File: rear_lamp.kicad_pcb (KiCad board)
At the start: 2 copper layers, 20.3 x 15.4 mm, 9 parts, among them J1 PWR, Q1 BD137

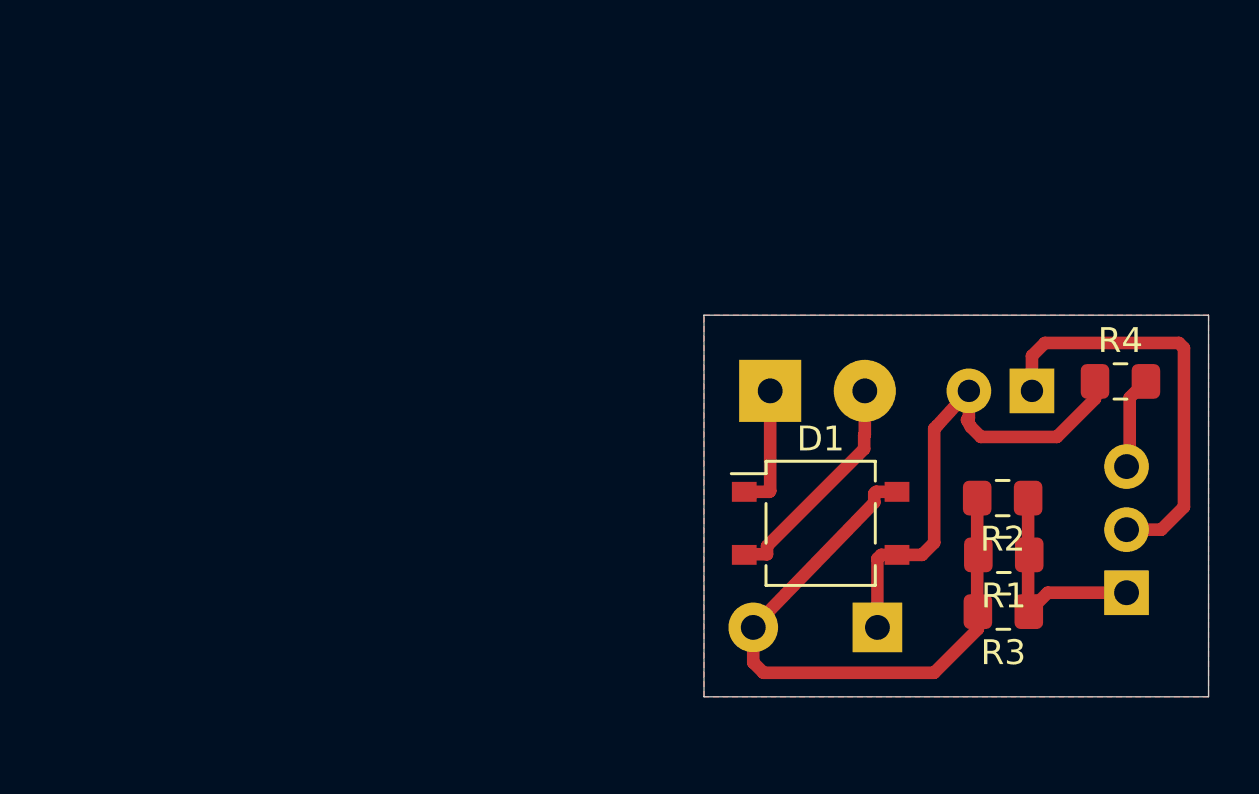
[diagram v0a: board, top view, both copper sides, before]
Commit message: discrete led driver
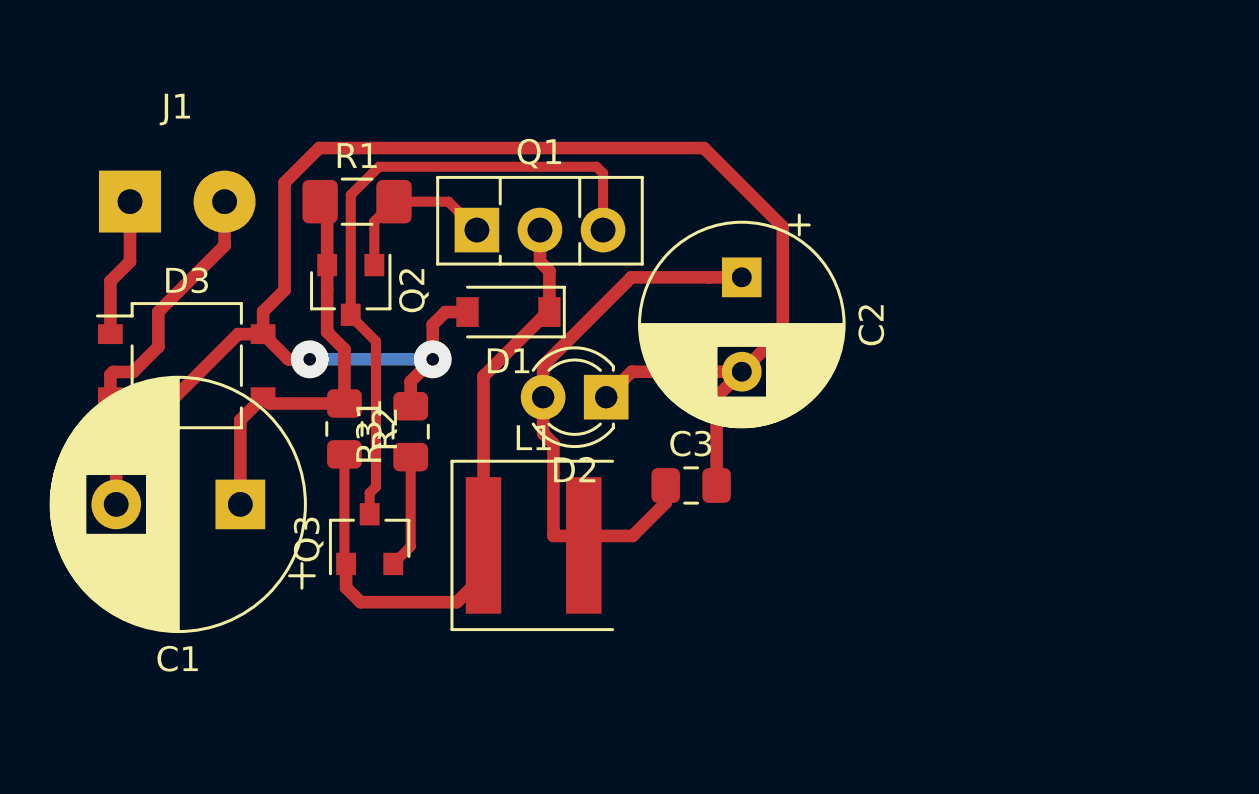
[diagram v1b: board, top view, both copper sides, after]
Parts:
- removed R3: 10R, Resistor_SMD:R_0805_2012Metric_Pad1.15x1.40mm_HandSolder
- removed R4: 10k, Resistor_SMD:R_0805_2012Metric_Pad1.15x1.40mm_HandSolder
- added C2: 200u, Capacitor_THT:CP_Radial_D8.0mm_P3.80mm, F.Cu at (61.2, 30.9)
- added C3: 1u, Capacitor_SMD:C_0805_2012Metric_Pad1.15x1.40mm_HandSolder, F.Cu at (59.2, 39.2)
- added D3: MB6S, Package_TO_SOT_SMD:TO-269AA, F.Cu at (38.9, 34.4)
- added L1: 47u, Inductor_SMD:L_Coilcraft_XAL60xx_6.36x6.56mm, F.Cu at (52.8, 41.7)
- added Q2: BC856, Package_TO_SOT_SMD:SOT-23, F.Cu at (45.5, 31.4)
- added Q3: BC847, Package_TO_SOT_SMD:SOT-23, F.Cu at (46.2, 41.4)
- added R31: 510, Resistor_SMD:R_0805_2012Metric_Pad1.15x1.40mm_HandSolder, F.Cu at (47.9, 37.1)
- C1, D2, J1: moved to F.Cu
- D1: value MB6S -> D_Schottky; footprint Package_TO_SOT_SMD:TO-269AA -> Diode_SMD:D_SOD-123
- Q1: value BD137 -> BD138; moved to F.Cu
- R1: value 10R -> 1R2; footprint Resistor_SMD:R_0805_2012Metric_Pad1.15x1.40mm_HandSolder -> Resistor_SMD:R_1206_3216Metric_Pad1.42x1.75mm_HandSolder
- R2: value 10R -> 10k
- moved Q1 30.0 mm to (50.5, 29.0), turned to 0 degrees
- moved R1 29.7 mm to (45.7, 27.8), turned to 0 degrees
- moved J1 26.9 mm to (36.6, 27.8)
- moved R2 26.7 mm to (45.2, 37.0), turned to 270 degrees
- moved C1 26.1 mm to (41.0, 40.0)
- moved D2 17.1 mm to (55.8, 35.7)
- moved D1 15.2 mm to (51.8, 32.3), turned to 180 degrees
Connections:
- D1 pad 2: Net-(D1-Pad2) -> GND
- D2 pad 1: Net-(D2-Pad1) -> GND
- D2 pad 2: VCC -> Net-(C2-Pad1)
- J1 pad 1: Net-(D1-Pad1) -> Net-(D3-Pad1)
- J1 pad 2: Net-(D1-Pad2) -> Net-(D3-Pad2)
- Q1 pad 2: Net-(D2-Pad1) -> Net-(D1-Pad1)
- R1 pad 1: Net-(Q1-Pad1) -> VCC
- R1 pad 2: GND -> Net-(Q1-Pad1)
- R2 pad 1: Net-(Q1-Pad1) -> VCC
- R2 pad 2: GND -> Net-(D1-Pad1)
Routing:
- net GND: track 25.0 -> 68.2 mm, vias 0 -> 2
- net Net-(Q1-Pad3): track 3.70 -> 26.4 mm
- net Net-(C2-Pad1): track 0.00 -> 22.5 mm
- net Net-(D1-Pad1): track 5.09 -> 26.8 mm
- net Net-(D2-Pad1): track 16.8 -> 0.00 mm
- net Net-(D3-Pad2): track 0.00 -> 10.3 mm
- net Net-(D1-Pad2): track 9.14 -> 0.00 mm
- net Net-(D3-Pad1): track 0.00 -> 5.66 mm
- net Net-(Q3-Pad2): track 0.00 -> 4.59 mm
- net VCC: track 20.0 -> 16.6 mm
- net Net-(Q1-Pad1): track 8.96 -> 6.70 mm
- removed copper zone on F.Cu, net GND
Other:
- board outline removed

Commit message: one plane
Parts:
- removed D3: MB6S, Package_TO_SOT_SMD:TO-269AA
- C1: footprint Capacitor_THT:CP_Radial_D10.0mm_P5.00mm -> Capacitor_THT:C_Axial_L5.1mm_D3.1mm_P12.50mm_Horizontal; moved to B.Cu
- C2, Q1: moved to B.Cu
- D1: footprint Diode_SMD:D_SOD-123 -> Diode_SMD:D_SMA_Handsoldering
- D2: footprint LED_THT:LED_D3.0mm -> LED_THT:LED_D4.0mm; moved to B.Cu
- L1: footprint Inductor_SMD:L_Coilcraft_XAL60xx_6.36x6.56mm -> Inductor_SMD:L_Bourns_SRP7028A_7.3x6.6mm
- moved C2 18.9 mm to (46.2, 42.4), turned to 90 degrees
- moved D2 16.7 mm to (44.1, 47.6), turned to 0 degrees
- moved J1 15.8 mm to (52.1, 24.6), turned to 180 degrees
- moved C1 15.6 mm to (43.8, 24.6), turned to 0 degrees
- moved C3 15.4 mm to (43.8, 40.6), turned to 90 degrees
- moved Q3 12.1 mm to (55.2, 33.4)
- moved R2 8.78 mm to (45.5, 28.2), turned to 0 degrees
- moved D1 6.69 mm to (52.9, 38.9)
- moved R3 5.21 mm to (51.6, 33.4)
- moved L1 3.68 mm to (52.8, 45.3), turned to 180 degrees
- moved R1 3.18 mm to (45.7, 31.0)
- moved Q2 3.17 mm to (45.5, 34.5)
- moved Q1 0.13 mm to (50.5, 28.8)
- renumbered R31 to R3
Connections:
- J1 pad 1: Net-(D3-Pad1) -> GND
- J1 pad 2: Net-(D3-Pad2) -> VCC
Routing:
- net Net-(D3-Pad2): track 10.3 -> 0.00 mm
- net Net-(Q1-Pad3): track 26.4 -> 16.2 mm
- net GND: track 68.2 -> 58.7 mm, vias 2 -> 0
- net Net-(C2-Pad1): track 22.5 -> 13.0 mm
- net Net-(D1-Pad1): track 26.8 -> 33.8 mm
- net Net-(D3-Pad1): track 5.66 -> 0.00 mm
- net VCC: track 16.6 -> 13.8 mm
- net Net-(Q3-Pad2): track 4.59 -> 5.93 mm
- added copper zone on F.Cu, net GND
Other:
- board outline added: 16.8 x 27.9 mm
- net class PWR removed
- net class pwr added: clearance 0.2, trace_width 0.508, via_dia 0.8, via_drill 0.4
- net class signal added: clearance 0.2, trace_width 0.4064, via_dia 0.8, via_drill 0.4

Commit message: small pcb
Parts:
- D2: footprint LED_THT:LED_D4.0mm -> Capacitor_THT:C_Axial_L5.1mm_D3.1mm_P12.50mm_Horizontal
- moved D1 4.83 mm to (56.6, 35.8), turned to 270 degrees
- moved L1 4.79 mm to (51.1, 40.9), turned to 270 degrees
- moved D2 3.96 mm to (43.7, 43.7)
- moved Q3 2.92 mm to (52.3, 33.5), turned to 180 degrees
- moved R3 2.54 mm to (49.0, 33.5), turned to 270 degrees
- moved C3 1.78 mm to (43.7, 38.9)
- moved C2 1.52 mm to (46.2, 40.9)
- moved Q2 1.08 mm to (44.7, 33.8)
- moved R1 0.92 mm to (45.2, 30.2)
- moved R2 0.91 mm to (44.7, 27.7)
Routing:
- net Net-(D1-Pad1): track 33.8 -> 28.5 mm
- net Net-(Q1-Pad3): track 16.2 -> 21.5 mm
- net Net-(C2-Pad1): track 13.0 -> 14.8 mm
- net Net-(Q3-Pad2): track 5.93 -> 4.54 mm
- net VCC: track 13.8 -> 12.7 mm
- net Net-(Q1-Pad1): track 7.19 -> 8.18 mm
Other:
- board size 16.8 x 27.9 mm -> 16.8 x 24.5 mm
